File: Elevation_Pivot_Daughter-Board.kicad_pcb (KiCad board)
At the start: 4 copper layers, 120 x 200 mm, 337 parts, among them IC1 TPS1H100BQPWPRQ1, IC2 TPS1H100BQPWPRQ1, J1 1827884, J12 CHASSIS / SHIELD, J2 DE9_Socket_MountingHoles, J20 DE9 FEMALE, J21 DE9 FEMALE, J22 DE9 MODBUS RTU, J3 DE9_Socket_MountingHoles, J30 SSW-115-01-S-D, J31 SSW-110-01-S-D, J4 DE9_Socket_MountingHoles, J5 DE9_Socket_MountingHoles, J6 DE9_Socket_MountingHoles, J7 DE9_Socket_MountingHoles, Q1 2N7002KQ-7, Q13 2N7002KQ-7, Q14 IRFS4115TRLPBF, Q15 IRFS4115TRLPBF, Q16 SSM3K361R,LF, Q2 2N7002KQ-7, Q3 2N7002KQ-7, Q4 2N7002KQ-7, Q5 2N7002KQ-7, Q6 2N7002KQ-7, Q7 2N7002KQ-7, U10 ISO6762DWR, U100 AM26LV32EIDR, U101 ISO7760FDWR, U102 TPD2E2U06QDBZRQ1, U103 TPD2E2U06QDBZRQ1, U104 TPD2E2U06QDBZRQ1, U105 TLV75533PDBVR, U11 TPD2E2U06QDBZRQ1, U110 AM26LV32EIDR, U112 TPD2E2U06QDBZRQ1, U113 TPD2E2U06QDBZRQ1, U114 TPD2E2U06QDBZRQ1, U12 TPD2E2U06QDBZRQ1, U13 ISO6763DWR, U14 R05CTE05S-R, U15 TCAN1051DRQ1, U16 ISO1432DWR, U160 ISO1410DWR, U17 ESD2CANFD24DBZRQ1, U18 ISO6762DWR, U19 TPD2E2U06QDBZRQ1, U2 ISO6762FQDWRQ1, U20 TPD2E2U06QDBZRQ1, U21 ADS1115BQDGSRQ1, U22 SN74LVC2G07DCKR(UMW), U23 TPS7A2450DBVR, U24 ISO1540DR, U25 TPS7A2450DBVR, U26 TPD1E10B09DPYR, U27 TPD1E10B09DPYR, U3 TPD2E2U06QDBZRQ1, U4 LTC4364IS-2-PBF, U5 TPD2E2U06QDBZRQ1, U6 TPD2E2U06QDBZRQ1, U7 ISO1432DWR, U8 TPD2E2U06QDBZRQ1, U9 TPD2E2U06QDBZRQ1

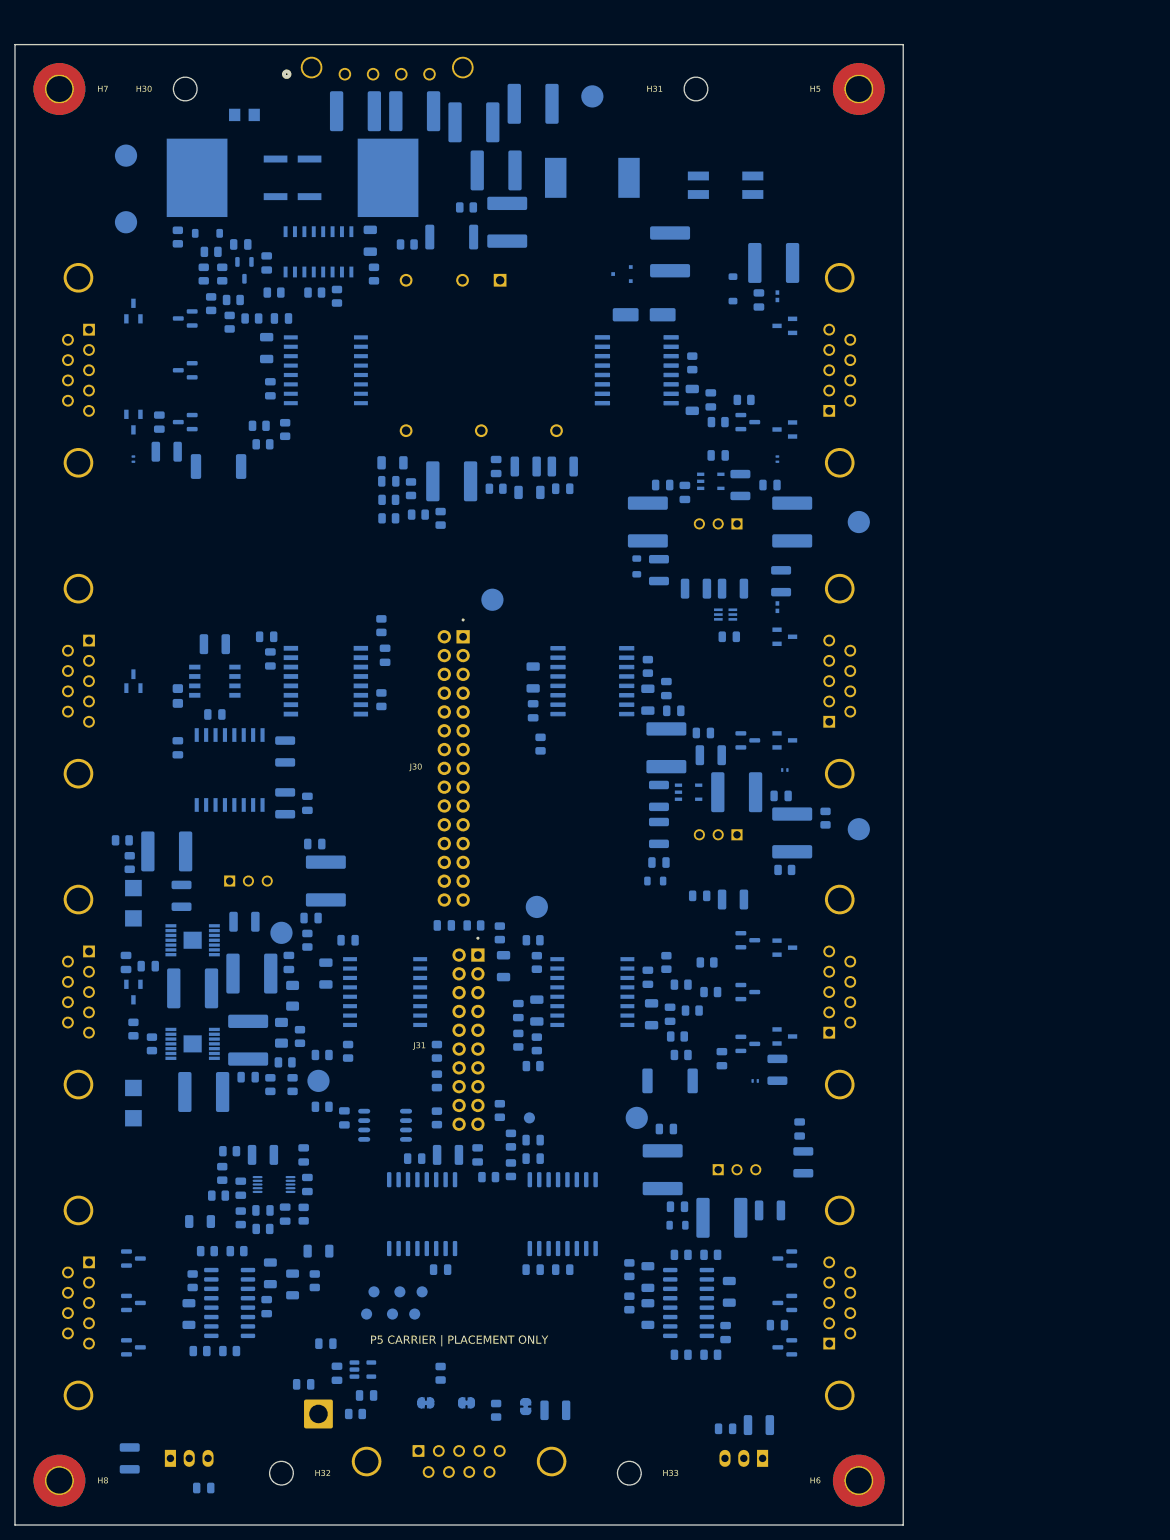
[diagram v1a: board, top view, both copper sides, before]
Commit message: Build P6 80x130 stack with redistributed SSI and stepper interfaces
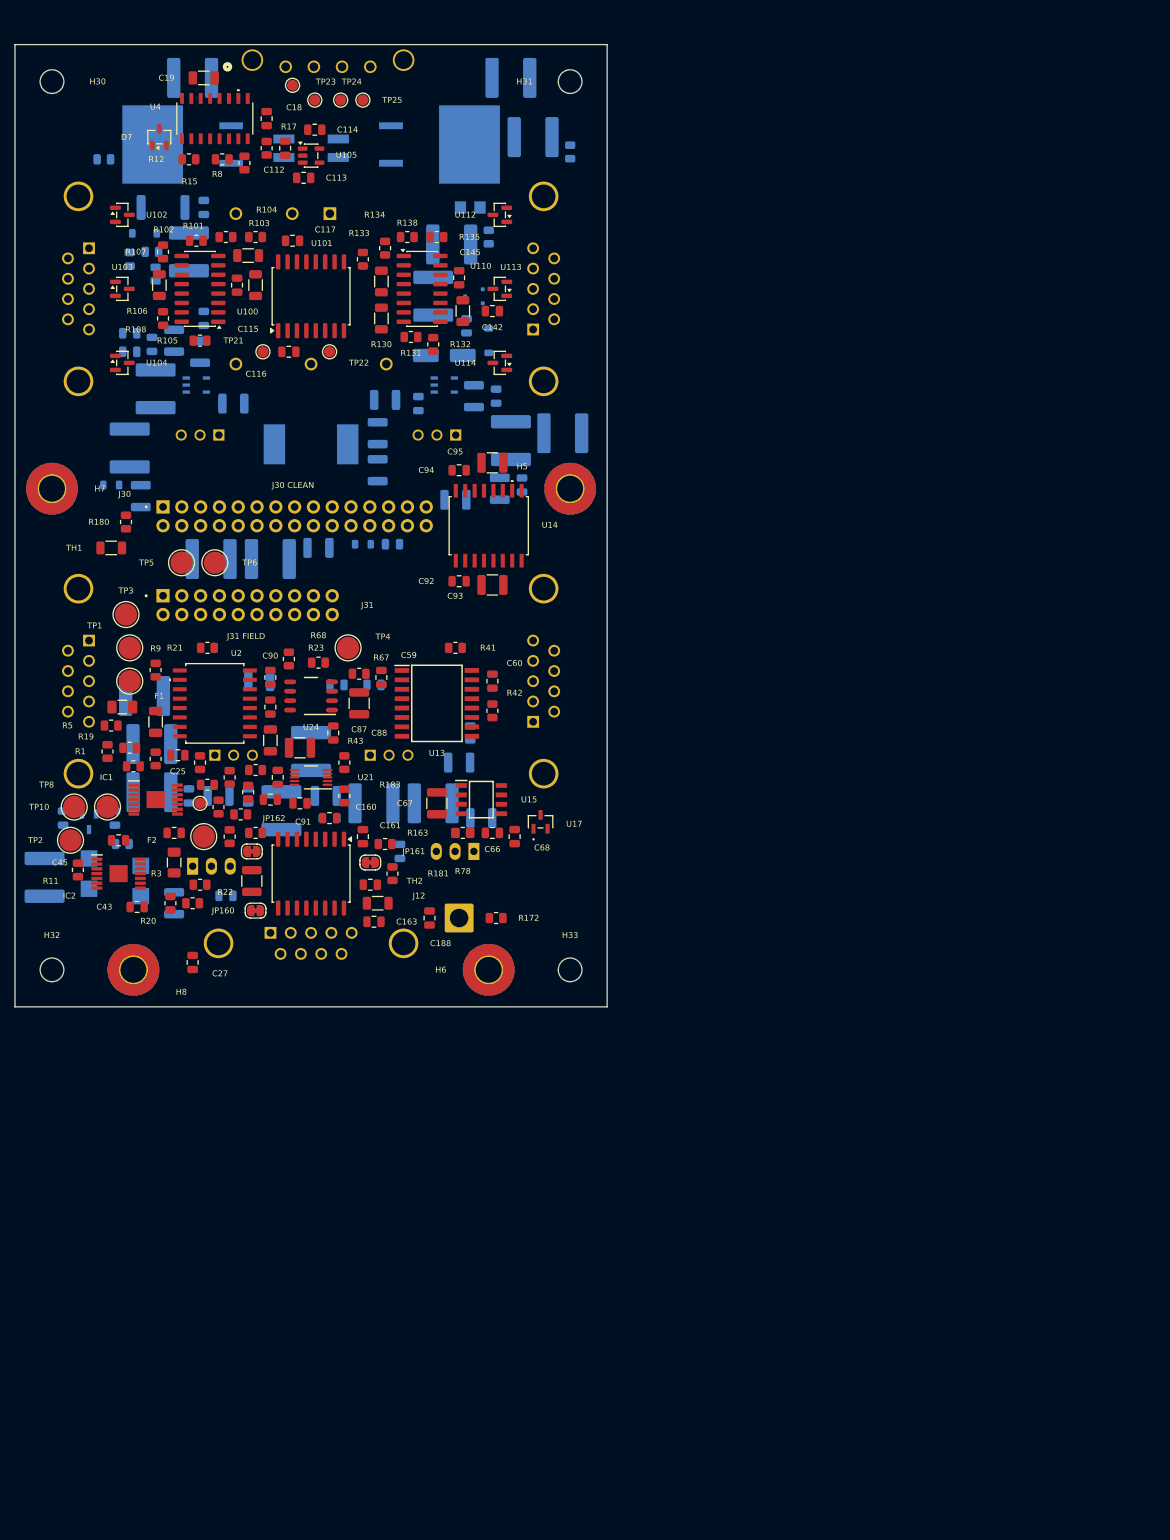
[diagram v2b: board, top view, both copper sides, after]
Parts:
- removed C17, C3: 10uF, Capacitor_SMD:C_2220_5750Metric
- removed C2, C38, C40, C53, C56, C57, C62, C65, C70, C71, C9, C97, C99: 0.1uF, Capacitor_SMD:C_0805_2012Metric
- removed C37, C42, C58, C6, C63, C64, C69, C72: 1uF, Capacitor_SMD:C_1206_3216Metric
- removed C51, C96: 10nF, Capacitor_SMD:C_0805_2012Metric
- removed C52, C98: 4.7uF, Capacitor_SMD:C_1210_3225Metric
- removed D1, D2, D3, D4: TPD1E10B06DPYR, TPD1E10B06DPYR:TPD1E10B06DPYR
- removed J2, J3, J4, J6: DE9_Socket_MountingHoles, Connector_Dsub:DSUB-9_Socket_Horizontal_P2.77x2.84mm_EdgePinOffset7.70mm_Housed_MountingHolesOffset9.12mm
- removed Q1, Q13, Q2, Q3, Q4, Q5, Q6, Q7: 2N7002KQ-7, Package_TO_SOT_SMD:SOT-23
- removed R2, R4: 120, Resistor_SMD:R_0805_2012Metric
- removed R27, R55: 4.7K, Resistor_SMD:R_0805_2012Metric
- removed R28, R29, R36, R37, R39, R40, R45, R46, R47, R48, R57, R58: 10K, Resistor_SMD:R_0805_2012Metric
- removed R30, R31, R32, R49, R50, R51: 100, Resistor_SMD:R_0805_2012Metric
- removed R33, R34, R35, R52, R53, R54, R61, R62: 47K, Resistor_SMD:R_0805_2012Metric
- removed R38, R56: 10, Resistor_SMD:R_2512_6332Metric_Pad1.40x3.35mm_HandSolder
- removed R59, R60: 2.2K, Resistor_SMD:R_0805_2012Metric
- removed U10, U18: ISO6762DWR, ISO6762QDWRQ1:ISO6762QDWRQ1
- removed U11, U12, U19, U20, U3, U6, U8, U9: TPD2E2U06QDBZRQ1, TPD2E2U06QDBZRQ1:SOT95P237X95-3N
- removed U16, U7: ISO1432DWR, ISO1432DWR:ISO1432DWR
- removed U22: SN74LVC2G07DCKR(UMW), SN74LVC2G07:SN74LVC2G07
- removed U26, U27: TPD1E10B09DPYR, TPD1E10B09DPYR:TPD1E10B09DPYR
- C112, C113, C114, C115, C116, C117, C142, C145, C160, C161, C162, C163, C18, C188, C19, C190, C191, C24, C25, C26, C27, C34, C4, C43, C45, C59, C60, C66, C67, C68, C87, C88, C89, C90, C91, C92, C93, C94, C95, D7, F1, F2, IC1, IC2, J12, JP160, JP161, JP162, R1, R100, R101, R102, R103, R104, R105, R106, R107, R108, R11, R12, R130, R131, R132, R133, R134, R135, R136, R137, R138, R15, R160, R161, R162, R163, R164, R165, R17, R172, R18, R180, R181, R182, R183, R19, R20, R21, R22, R23, R24, R25, R3, R41, R42, R43, R44, R5, R65, R66, R67, R68, R78, R8, R9, TH1, TH2, TP1, TP10, TP2, TP20, TP21, TP22, TP23, TP24, TP25, TP3, TP30, TP4, TP5, TP6, TP7, TP8, TP9, U100, U101, U102, U103, U104, U105, U110, U112, U113, U114, U13, U14, U15, U160, U17, U2, U21, U24, U4: moved to F.Cu
- moved C114 171.1 mm to (60.5, 31.5)
- moved TP23 164.1 mm to (60.5, 27.5)
- moved TP24 164.1 mm to (64.0, 27.5)
- moved TP25 164.1 mm to (67.0, 27.5)
- moved U105 164.1 mm to (60.0, 35.0)
- moved TP20 163.4 mm to (57.5, 25.5)
- moved C112 161.6 mm to (56.5, 34.0), turned to -90 degrees
- moved C113 161.6 mm to (59.0, 38.0), turned to 0 degrees
- moved C145 147.0 mm to (80.0, 51.5), turned to -90 degrees
- moved U112 146.2 mm to (85.5, 43.0)
- moved R137 145.5 mm to (67.0, 49.0), turned to -90 degrees
- moved J21 142.7 mm to (90.0, 58.5)
- moved R134 142.4 mm to (73.0, 46.0), turned to 180 degrees
- moved R135 142.4 mm to (77.0, 46.0)
- moved C142 142.3 mm to (84.5, 56.0), turned to 0 degrees
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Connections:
- net /ADS1115/PORT_BRAKE_CURR renamed PORT_BRAKE_CURR
- net /ADS1115/STAR_BRAKE_CURR renamed STAR_BRAKE_CURR
- net /Pivot_Encoder_Port/STAR_ENC_A_RX renamed STAR_ENC_A_RX
- net /Pivot_Encoder_Port/STAR_ENC_B_RX renamed STAR_ENC_B_RX
- net /Pivot_Encoder_Port/STAR_ENC_Z_RX renamed STAR_ENC_Z_RX
- J30 pad 10: /Controller_Interface/STAR_STR8_FAULT -> STAR_ENC_A
- J30 pad 11: GND_STM32 -> STAR_ENC_B
- J30 pad 12: GND_STM32 -> STAR_ENC_Z
- J30 pad 13: /Controller_Interface/PORT_SSI_CLK -> GND_STM32
- J30 pad 14: /Controller_Interface/STAR_SSI_CLK -> GND_STM32
- J30 pad 15: /Controller_Interface/PORT_SSI_DATA -> STM32_SCL
- J30 pad 16: /Controller_Interface/STAR_SSI_DATA -> STM32_SDA
- J30 pad 17: /Controller_Interface/PORT_ENC_PRESET_N -> TX_CAN
- J30 pad 18: /Controller_Interface/STAR_ENC_PRESET_N -> RX_CAN
- J30 pad 19: /Brakes/PORT_BRAKE_RELEASE_CMD -> Silent_Mode
- J30 pad 20: /Brakes/STAR_BRAKE_RELEASE_CMD -> PIVOT_MODBUS_TX
- J30 pad 21: GND_STM32 -> PIVOT_MODBUS_RX
- J30 pad 22: GND_STM32 -> PIVOT_MODBUS_DE
- J30 pad 23: /Brakes/HOME_POS -> CTRL_NRST
- J30 pad 24: /Brakes/E_STOP_OK -> GND_STM32
- J30 pad 27: GND_STM32 -> +3V3_STM32
- J30 pad 28: GND_STM32 -> +3V3_STM32
- J30 pad 29: +3V3_STM32 -> GND_STM32
- J30 pad 3: /Controller_Interface/PORT_STR8_STEP_CMD -> PORT_BRAKE_RELEASE_CMD
- J30 pad 30: +3V3_STM32 -> GND_STM32
- J30 pad 4: /Controller_Interface/STAR_STR8_STEP_CMD -> STAR_BRAKE_RELEASE_CMD
- J30 pad 5: /Controller_Interface/PORT_STR8_DIR_CMD -> HOME_POS
- J30 pad 6: /Controller_Interface/STAR_STR8_DIR_CMD -> E_STOP_OK
- J30 pad 7: /Controller_Interface/PORT_STR8_DISABLE -> PORT_ENC_A
- J30 pad 8: /Controller_Interface/STAR_STR8_DISABLE -> PORT_ENC_B
- J30 pad 9: /Controller_Interface/PORT_STR8_FAULT -> PORT_ENC_Z
- J31 pad 1: /Pivot_Encoder_Port/PORT_ENC_A -> -BATT
- J31 pad 10: GND_STM32 -> +6.5V_ENC_PORT
- J31 pad 11: /ADS1115/STM32_SCL -> +5V_ENC_PORT
- J31 pad 12: /ADS1115/STM32_SDA -> +5V_ENC_PORT
- J31 pad 13: /PIVOT_MODBUS_TX -> -BATT
- J31 pad 14: /PIVOT_MODBUS_RX -> -BATT
- J31 pad 15: /Controller_Interface/TX_CAN -> +6.5V_ENC_STAR
- J31 pad 16: /Controller_Interface/RX_CAN -> +6.5V_ENC_STAR
- J31 pad 17: /Controller_Interface/Silent_Mode -> +5V_ENC_STAR
- J31 pad 18: /PIVOT_MODBUS_DE -> +5V_ENC_STAR
- J31 pad 19: CTRL_NRST -> -BATT
- J31 pad 2: /Pivot_Encoder_Port/PORT_ENC_B -> -BATT
- J31 pad 20: GND_STM32 -> -BATT
- J31 pad 3: GND_STM32 -> -BATT
- J31 pad 4: GND_STM32 -> -BATT
- J31 pad 5: /Pivot_Encoder_Port/STAR_ENC_A -> +5V_FIELD
- J31 pad 6: /Pivot_Encoder_Port/STAR_ENC_B -> +5V_FIELD
- J31 pad 7: /Pivot_Encoder_Port/PORT_ENC_Z -> -BATT
- J31 pad 8: /Pivot_Encoder_Port/STAR_ENC_Z -> -BATT
- J31 pad 9: GND_STM32 -> +6.5V_ENC_PORT
- R160 pad 2: /PIVOT_MODBUS_TX -> PIVOT_MODBUS_TX
- R161 pad 2: /PIVOT_MODBUS_RX -> PIVOT_MODBUS_RX
- R162 pad 1: /PIVOT_MODBUS_DE -> PIVOT_MODBUS_DE
- R23 pad 2: /Brakes/STAR_BRAKE_RELEASE_CMD -> STAR_BRAKE_RELEASE_CMD
- R24 pad 2: /Brakes/PORT_BRAKE_RELEASE_CMD -> PORT_BRAKE_RELEASE_CMD
- R41 pad 2: /Controller_Interface/Silent_Mode -> Silent_Mode
- R42 pad 2: /Controller_Interface/TX_CAN -> TX_CAN
- R43 pad 2: /Brakes/E_STOP_OK -> E_STOP_OK
- R44 pad 2: /Brakes/HOME_POS -> HOME_POS
- R67 pad 1: /ADS1115/STM32_SDA -> STM32_SDA
- R68 pad 1: /ADS1115/STM32_SCL -> STM32_SCL
- TP20 pad 1: /Pivot_Encoder_Port/PORT_ENC_A -> PORT_ENC_A
- TP21 pad 1: /Pivot_Encoder_Port/PORT_ENC_B -> PORT_ENC_B
- TP22 pad 1: /Pivot_Encoder_Port/PORT_ENC_Z -> PORT_ENC_Z
- TP23 pad 1: /Pivot_Encoder_Port/STAR_ENC_A -> STAR_ENC_A
- TP24 pad 1: /Pivot_Encoder_Port/STAR_ENC_B -> STAR_ENC_B
- TP25 pad 1: /Pivot_Encoder_Port/STAR_ENC_Z -> STAR_ENC_Z
- U101 pad 10: /Pivot_Encoder_Port/STAR_ENC_Z -> STAR_ENC_Z
- U101 pad 11: /Pivot_Encoder_Port/STAR_ENC_B -> STAR_ENC_B
- U101 pad 12: /Pivot_Encoder_Port/STAR_ENC_A -> STAR_ENC_A
- U101 pad 13: /Pivot_Encoder_Port/PORT_ENC_Z -> PORT_ENC_Z
- U101 pad 14: /Pivot_Encoder_Port/PORT_ENC_B -> PORT_ENC_B
- U101 pad 15: /Pivot_Encoder_Port/PORT_ENC_A -> PORT_ENC_A
- U13 pad 2: /Controller_Interface/Silent_Mode -> Silent_Mode
- U13 pad 3: /Controller_Interface/TX_CAN -> TX_CAN
- U13 pad 5: /Controller_Interface/RX_CAN -> RX_CAN
- U160 pad 3: /PIVOT_MODBUS_RX -> PIVOT_MODBUS_RX
- U160 pad 4: /PIVOT_MODBUS_DE -> PIVOT_MODBUS_DE
- U160 pad 5: /PIVOT_MODBUS_DE -> PIVOT_MODBUS_DE
- U160 pad 6: /PIVOT_MODBUS_TX -> PIVOT_MODBUS_TX
- U2 pad 2: /Brakes/PORT_BRAKE_RELEASE_CMD -> PORT_BRAKE_RELEASE_CMD
- U2 pad 3: /Brakes/STAR_BRAKE_RELEASE_CMD -> STAR_BRAKE_RELEASE_CMD
- U2 pad 6: /Brakes/HOME_POS -> HOME_POS
- U2 pad 7: /Brakes/E_STOP_OK -> E_STOP_OK
- U24 pad 2: /ADS1115/STM32_SDA -> STM32_SDA
- U24 pad 3: /ADS1115/STM32_SCL -> STM32_SCL
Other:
- board size 120 x 200 mm -> 80 x 130 mm
- board text added: "J30 CLEAN"
- board text added: "J31 FIELD"
- board text added: "P6 80 x 130 | UNROUTED"
- board text removed: "120 x 200 mm / 4 layers / NO ROUTING"
- board text removed: "OUTWARD FACE: BOTTOM"
- board text removed: "P5 CARRIER | PLACEMENT ONLY"
- board text removed: "PORT SSI"
- board text removed: "PORT STEP"
- board text removed: "STAR MOTOR"
- board text removed: "STAR SSI"
- board text removed: "STAR STEP"
